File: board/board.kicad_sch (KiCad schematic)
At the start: 1 part

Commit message: initial
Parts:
- added J1: 010_UART, on_edge:on_edge_2x05_device, symbol put_on_edge:010_UART
- added J2: Conn_01x03_Male, Connector_PinHeader_2.54mm:PinHeader_1x03_P2.54mm_Vertical, symbol Connector:Conn_01x03_Male
- added R1: d.n.p, Resistor_SMD:R_0603_1608Metric, symbol Device:R_Small
- added R2, R3: 0R, Resistor_SMD:R_0603_1608Metric, symbol Device:R_Small
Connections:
- new net: J1.6 (CS/EN), R2.1
- new net: J1.5 (INT), R1.1
- new net +3.3V: J1.9 (3.3V)
- new net GND: J1.1 (GND), J2.1 (Pin_1)
- new net implementation/A: J2.2 (Pin_2)
- new net implementation/B: J2.3 (Pin_3)
- new net implementation/RX: J1.2 (TX)
- new net implementation/RX_EN: R1.2, R3.2
- new net implementation/TX: J1.3 (RX)
- new net implementation/TX_EN: R2.2, R3.1
- no-connect marks 0 -> 2
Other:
- sheet implementation ports: added 3.3V, A, B, GND, RX, RX_EN, TX, TX_EN; removed none
- note removed: "Input connectors go here"
- note removed: "Output connectors go here"

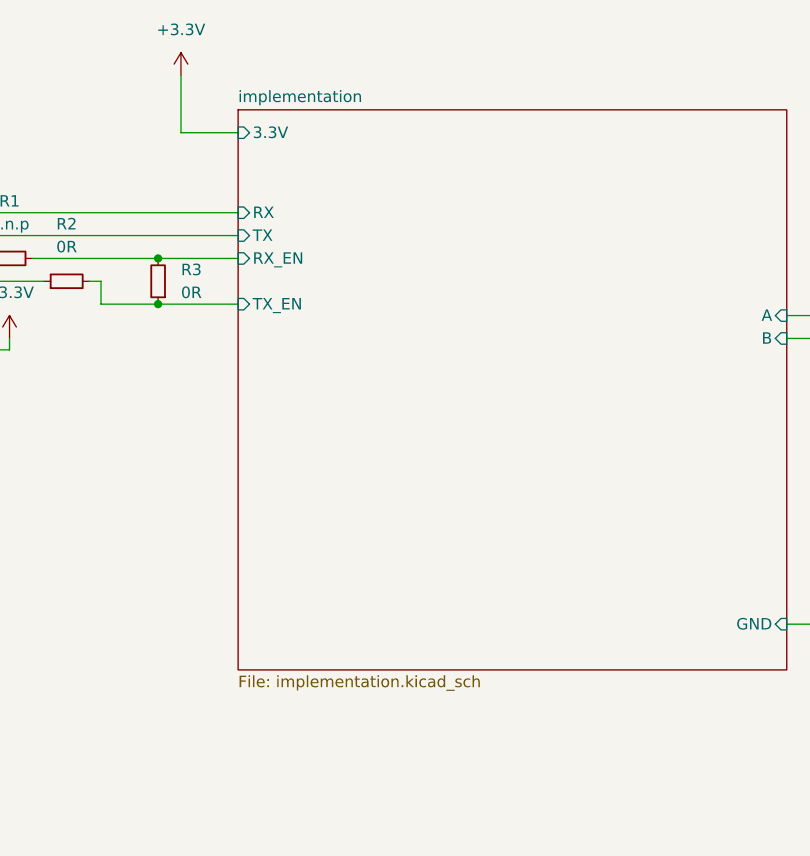
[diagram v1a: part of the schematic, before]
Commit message: changed implementation.kicad_sch to max485.kicad_sch in order to avoid clashing on the name implementation with other edgies in a composition
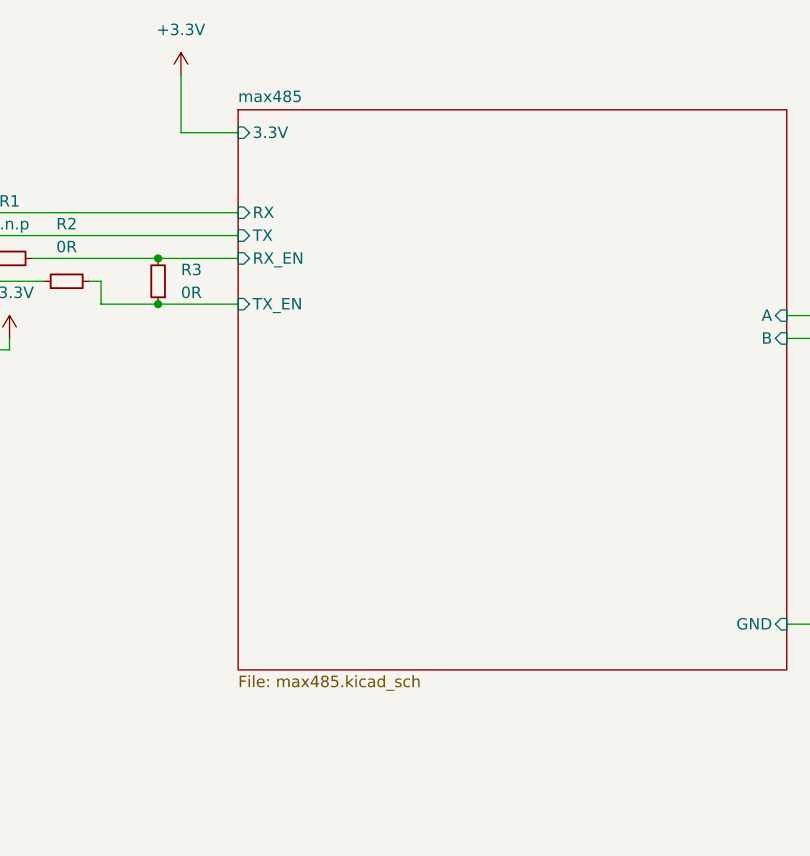
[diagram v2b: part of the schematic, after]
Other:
- sheet implementation renamed max485
- sheet max485: file implementation.kicad_sch -> max485.kicad_sch
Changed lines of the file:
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@@
     (stroke (width 0.1524) (type solid) (color 0 0 0 0))
     (fill (color 0 0 0 0.0000))
-    (property "Sheet name" "implementation" (id 0) (at 114.3 71.6784 0)
+    (property "Sheet name" "max485" (id 0) (at 114.3 71.6784 0)
       (effects (font (size 1.27 1.27)) (justify left bottom))
     )
-    (property "Sheet file" "implementation.kicad_sch" (id 1) (at 114.3 135.2046 0)
+    (property "Sheet file" "max485.kicad_sch" (id 1) (at 114.3 135.2046 0)
       (effects (font (size 1.27 1.27)) (justify left top))
     )

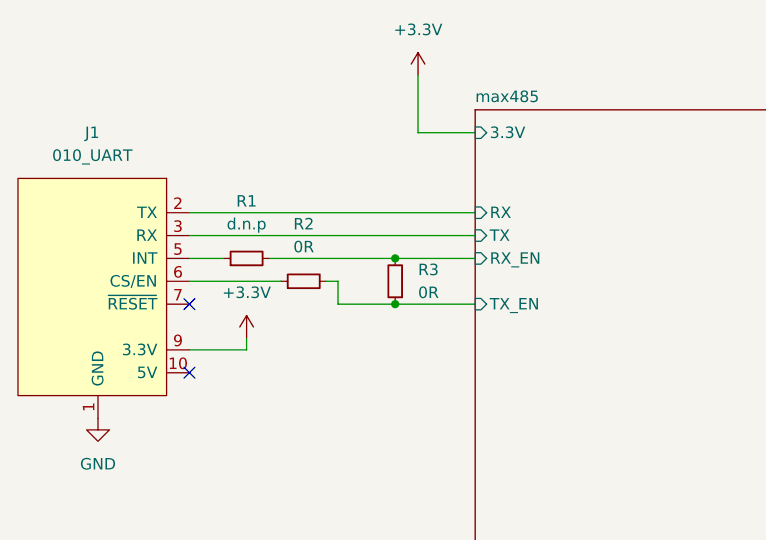
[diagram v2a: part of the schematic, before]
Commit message: changed supply to 5V and fixed up silkscreen
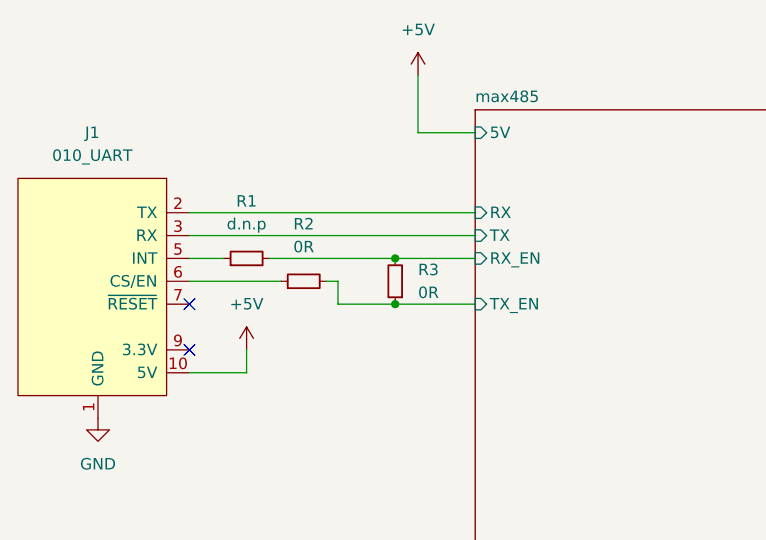
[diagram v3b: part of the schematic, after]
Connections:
- net +5V: now reaches J1.10 (5V)
- net +3.3V: no longer names the net of J1.9 (3.3V)
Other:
- sheet max485 ports: added 5V; removed 3.3V
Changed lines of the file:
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@@
   )
   (no_connect (at 82.55 93.98))
-  (no_connect (at 82.55 101.6))
+  (no_connect (at 82.55 99.06))
   (wire (pts (xy 82.55 91.44) (xy 92.71 91.44))
     (stroke (width 0) (type default) (color 0 0 0 0))
@@
     (stroke (width 0) (type default) (color 0 0 0 0))
   )
+  (wire (pts (xy 88.9 101.6) (xy 88.9 99.06))
+    (stroke (width 0) (type default) (color 0 0 0 0))
+  )
   (wire (pts (xy 175.26 97.79) (xy 193.04 97.79))
     (stroke (width 0) (type default) (color 0 0 0 0))
@@
     (stroke (width 0) (type default) (color 0 0 0 0))
   )
-  (wire (pts (xy 88.9 99.06) (xy 88.9 97.79))
-    (stroke (width 0) (type default) (color 0 0 0 0))
-  )
   (wire (pts (xy 180.34 92.71) (xy 180.34 129.54))
     (stroke (width 0) (type default) (color 0 0 0 0))
@@
     (stroke (width 0) (type default) (color 0 0 0 0))
   )
-  (wire (pts (xy 82.55 99.06) (xy 88.9 99.06))
+  (wire (pts (xy 82.55 101.6) (xy 88.9 101.6))
     (stroke (width 0) (type default) (color 0 0 0 0))
   )
@@
     (stroke (width 0) (type default) (color 0 0 0 0))
   )
-  (symbol (lib_id "power:+3.3V") (at 107.95 68.58 0) (unit 1)
+  (symbol (lib_id "Device:R_Small") (at 105.41 91.44 180) (unit 1)
+    (in_bom yes) (on_board yes) (fields_autoplaced)
+    (property "Reference" "R3" (id 0) (at 107.95 90.1699 0)
+      (effects (font (size 1.27 1.27)) (justify right))
+    )
+    (property "Value" "0R" (id 1) (at 107.95 92.7099 0)
+      (effects (font (size 1.27 1.27)) (justify right))
+    )
+    (property "Footprint" "Resistor_SMD:R_0603_1608Metric" (id 2) (at 105.41 91.44 0)
+      (effects (font (size 1.27 1.27)) hide)
+    )
+    (property "Datasheet" "~" (id 3) (at 105.41 91.44 0)
+      (effects (font (size 1.27 1.27)) hide)
+    )
+    (pin "1")
+    (pin "2")
+  )
+  (symbol (lib_id "power:+5V") (at 107.95 68.58 0) (unit 1)
     (in_bom yes) (on_board yes) (fields_autoplaced)
     (property "Reference" "#PWR0104" (id 0) (at 107.95 72.39 0)
       (effects (font (size 1.27 1.27)) hide)
     )
-    (property "Value" "+3.3V" (id 1) (at 107.95 63.5 0))
+    (property "Value" "+5V" (id 1) (at 107.95 63.5 0))
     (property "Footprint" "" (id 2) (at 107.95 68.58 0)
       (effects (font (size 1.27 1.27)) hide)
@@
     )
     (pin "1")
-  )
-  (symbol (lib_id "Device:R_Small") (at 105.41 91.44 180) (unit 1)
-    (in_bom yes) (on_board yes) (fields_autoplaced)
-    (property "Reference" "R3" (id 0) (at 107.95 90.1699 0)
-      (effects (font (size 1.27 1.27)) (justify right))
-    )
-    (property "Value" "0R" (id 1) (at 107.95 92.7099 0)
-      (effects (font (size 1.27 1.27)) (justify right))
-    )
-    (property "Footprint" "Resistor_SMD:R_0603_1608Metric" (id 2) (at 105.41 91.44 0)
-      (effects (font (size 1.27 1.27)) hide)
-    )
-    (property "Datasheet" "~" (id 3) (at 105.41 91.44 0)
-      (effects (font (size 1.27 1.27)) hide)
-    )
-    (pin "1")
-    (pin "2")
   )
   (symbol (lib_id "Device:R_Small") (at 95.25 91.44 90) (unit 1)
@@
     (pin "2")
   )
-  (symbol (lib_id "power:+3.3V") (at 88.9 97.79 0) (unit 1)
-    (in_bom yes) (on_board yes) (fields_autoplaced)
-    (property "Reference" "#PWR0103" (id 0) (at 88.9 101.6 0)
-      (effects (font (size 1.27 1.27)) hide)
-    )
-    (property "Value" "+3.3V" (id 1) (at 88.9 92.71 0))
-    (property "Footprint" "" (id 2) (at 88.9 97.79 0)
-      (effects (font (size 1.27 1.27)) hide)
-    )
-    (property "Datasheet" "" (id 3) (at 88.9 97.79 0)
-      (effects (font (size 1.27 1.27)) hide)
-    )
-    (pin "1")
-  )
   (symbol (lib_id "Connector:Conn_01x03_Male") (at 198.12 95.25 0) (mirror y) (unit 1)
     (in_bom yes) (on_board yes) (fields_autoplaced)
@@
       (effects (font (size 1.27 1.27)) hide)
     )
+  )
+  (symbol (lib_id "power:+5V") (at 88.9 99.06 0) (unit 1)
+    (in_bom yes) (on_board yes) (fields_autoplaced)
+    (property "Reference" "#PWR0103" (id 0) (at 88.9 102.87 0)
+      (effects (font (size 1.27 1.27)) hide)
+    )
+    (property "Value" "+5V" (id 1) (at 88.9 93.98 0))
+    (property "Footprint" "" (id 2) (at 88.9 99.06 0)
+      (effects (font (size 1.27 1.27)) hide)
+    )
+    (property "Datasheet" "" (id 3) (at 88.9 99.06 0)
+      (effects (font (size 1.27 1.27)) hide)
+    )
+    (pin "1")
   )
   (symbol (lib_id "put_on_edge:010_UART") (at 71.12 92.71 0) (mirror y) (unit 1)
@@
       (effects (font (size 1.27 1.27)) (justify left))
     )
-    (pin "3.3V" input (at 114.3 74.93 180)
+    (pin "5V" input (at 114.3 74.93 180)
       (effects (font (size 1.27 1.27)) (justify left))
     )
@@
       (reference "#PWR0102") (unit 1) (value "GND") (footprint "")
     )
-    (path "/6b0bd7eb-cf64-46c4-a698-29e536985b63"
-      (reference "#PWR0103") (unit 1) (value "+3.3V") (footprint "")
-    )
-    (path "/18aad469-a99f-4a9f-af30-61b914eec257"
-      (reference "#PWR0104") (unit 1) (value "+3.3V") (footprint "")
+    (path "/ba9beb0b-2da0-42d9-8d26-dc67ae35d1da"
+      (reference "#PWR0103") (unit 1) (value "+5V") (footprint "")
+    )
+    (path "/50f9b80d-b7aa-4a20-979f-344b3705d7b0"
+      (reference "#PWR0104") (unit 1) (value "+5V") (footprint "")
     )
     (path "/767ce4c6-0e55-4543-92f0-34cb8237a544/485a425d-9408-4dd6-9843-08652d513cbd"
-      (reference "C1") (unit 1) (value "100nF") (footprint "Resistor_SMD:R_0603_1608Metric")
+      (reference "C1") (unit 1) (value "100nF") (footprint "Capacitor_SMD:C_0603_1608Metric")
     )
     (path "/d9b73637-b257-4c21-9dfa-93c3e077891f"
